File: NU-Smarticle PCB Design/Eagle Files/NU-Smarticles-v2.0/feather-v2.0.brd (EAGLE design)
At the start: 48.3 x 22.9 mm, 43 parts, among them CON100 12XFFCMOLEX_51281, IC1 ATMEGA328P, Q1 DMG341, SW1 KMR2, U1 MCP73831T-2ACI/OT, U2 AP2112-3.3, U3 CP2104, X1 20329, Y1 RESONATORMU

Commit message: update inventory, eagle
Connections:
- removed net N$13: U$1.14
- removed net N$14: U$1.7
- removed net N$15: U$1.6
- net 3.3V: now also U$1.14
- net GND: now also U$1.6, U$1.7
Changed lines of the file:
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@@
 <wire x1="1.937" y1="10.68" x2="1.778" y2="10.839" width="0.254" layer="1"/>
 <wire x1="1.778" y1="10.839" x2="1.778" y2="11.43" width="0.254" layer="1"/>
+<contactref element="U$1" pad="6"/>
+<contactref element="U$1" pad="7"/>
 <wire x1="1.4725" y1="17.3355" x2="2.037" y2="15.03" width="0" layer="19" extent="1-1"/>
 <wire x1="4.41" y1="7.83" x2="4.837" y2="8.13" width="0" layer="19" extent="1-1"/>
+<wire x1="40.61" y1="14.99" x2="38.1" y2="14.478" width="0" layer="19" extent="1-1"/>
 </signal>
 <signal name="VBUS">
@@
 <via x="36.9926" y="11.41791875" extent="1-16" drill="0.5"/>
 <wire x1="22.35" y1="6.209" x2="22.35" y2="5.59" width="0.254" layer="16"/>
+<contactref element="U$1" pad="14"/>
+<wire x1="43.21" y1="15.49" x2="43.21" y2="14.99" width="0" layer="19" extent="1-1"/>
 </signal>
 <signal name="RESET">
@@
 <wire x1="44.387" y1="10.16" x2="42.926" y2="10.16" width="0.254" layer="1"/>
 </signal>
-<signal name="N$13">
-<contactref element="U$1" pad="14"/>
-</signal>
-<signal name="N$14">
-<contactref element="U$1" pad="7"/>
-</signal>
-<signal name="N$15">
-<contactref element="U$1" pad="6"/>
-</signal>
 <signal name="N$16">

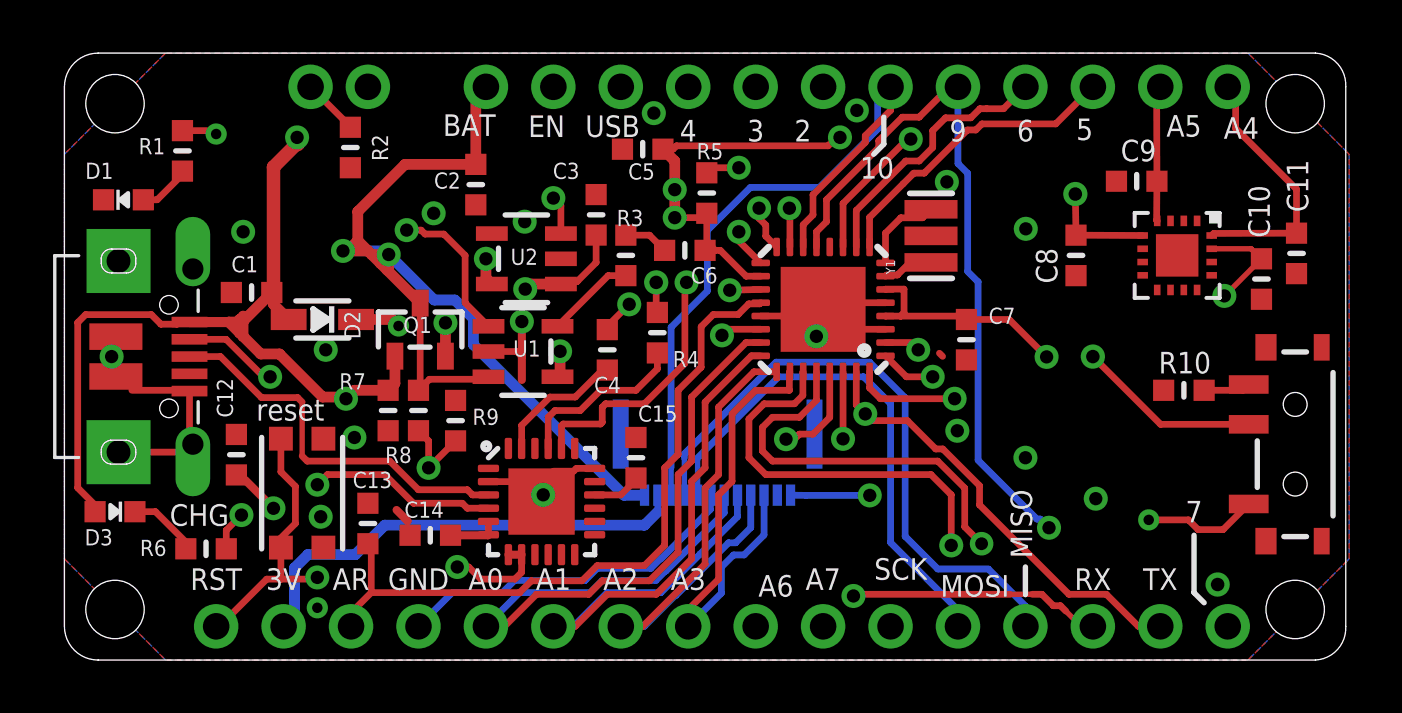
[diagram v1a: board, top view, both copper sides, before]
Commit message: delete cam outputs
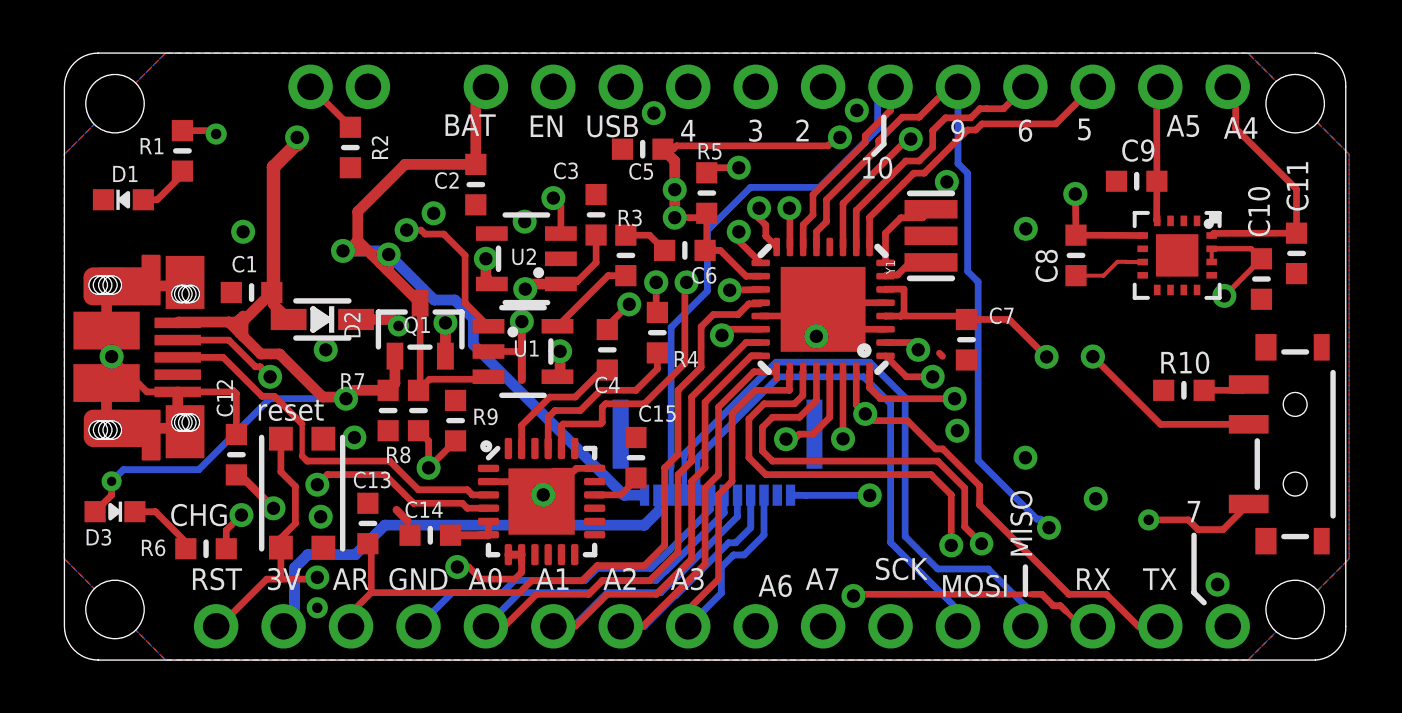
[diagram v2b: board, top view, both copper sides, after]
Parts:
- IC1: value ATMEGA328P -> ATMEGA328PB
- X1: value 20329 -> AMP FCI 10103594-0001LF; device NU-Smarticle v2:4UCONN_20329_V2 -> NU-Smarticle v2:USB-MICROB-PTH
- Y1: value RESONATORMU -> CSTNE8M00GH5C000R0
- moved X1 1.00 mm to (2.94, 11.4)
- renumbered U$1 to U4
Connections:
- net GND: now also X1.P$1, X1.P$10, X1.P$12, X1.P$2, X1.P$3, X1.P$4, X1.P$6, X1.P$8, X1.SHEILD2, X1.SHIELD, X1.SHIELD3, X1.SHIELD4; no longer X1.BASE@1, X1.BASE@2, X1.SPRT@1, X1.SPRT@2, X1.SPRT@3, X1.SPRT@4
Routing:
- net GND: track 39.9 -> 55.0 mm
- net 3.3V: track 97.3 -> 97.8 mm
- net VBUS: track 67.6 -> 67.7 mm, vias 4 -> 5
